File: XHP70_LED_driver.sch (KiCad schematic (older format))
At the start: 24 parts, among them U1 TPS61088, U2 INA181

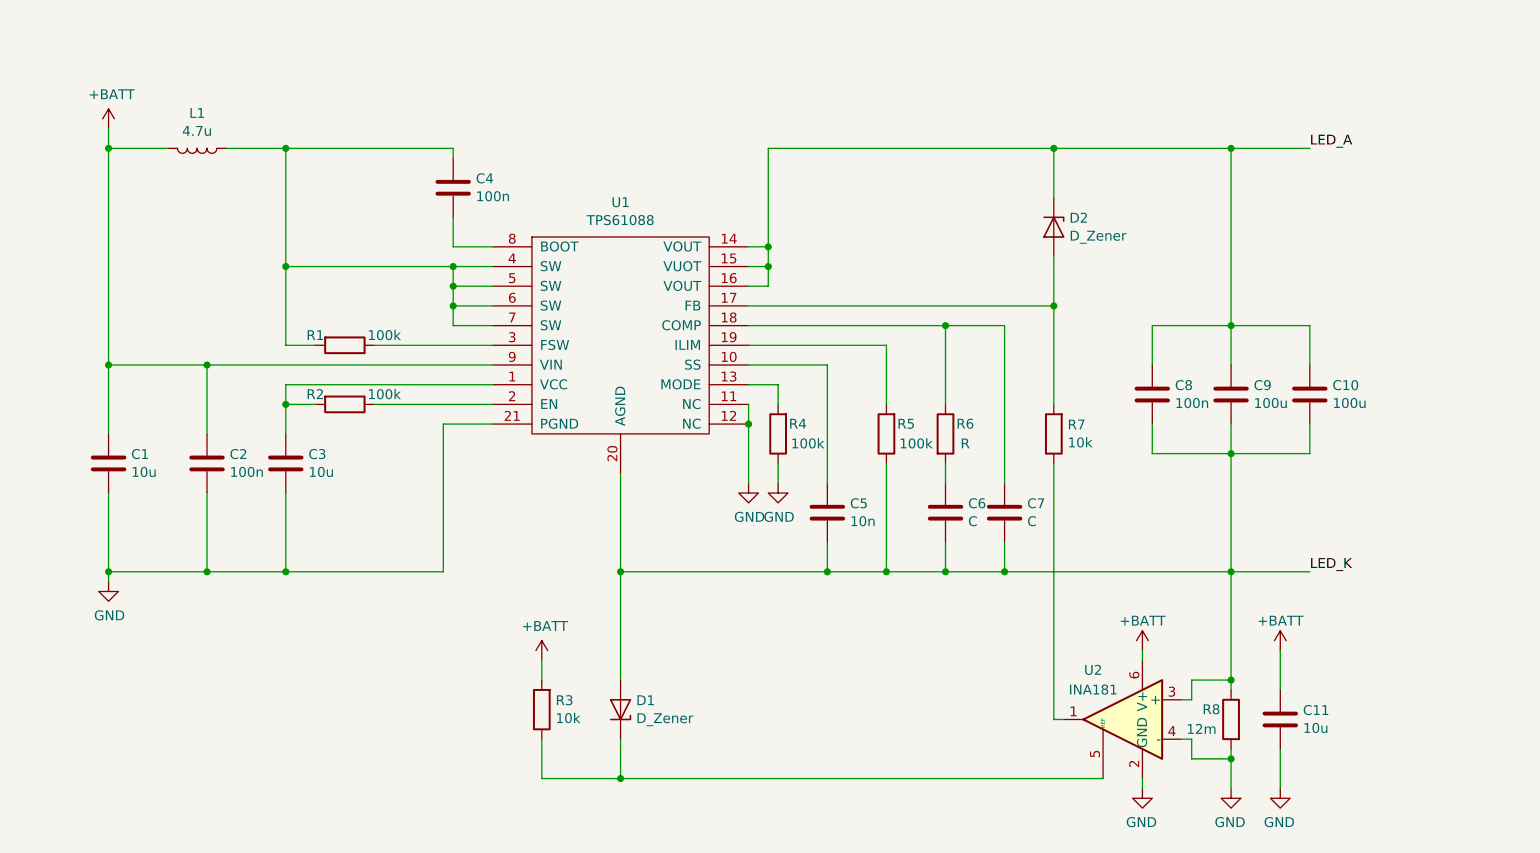
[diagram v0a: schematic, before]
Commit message: added microcontroller
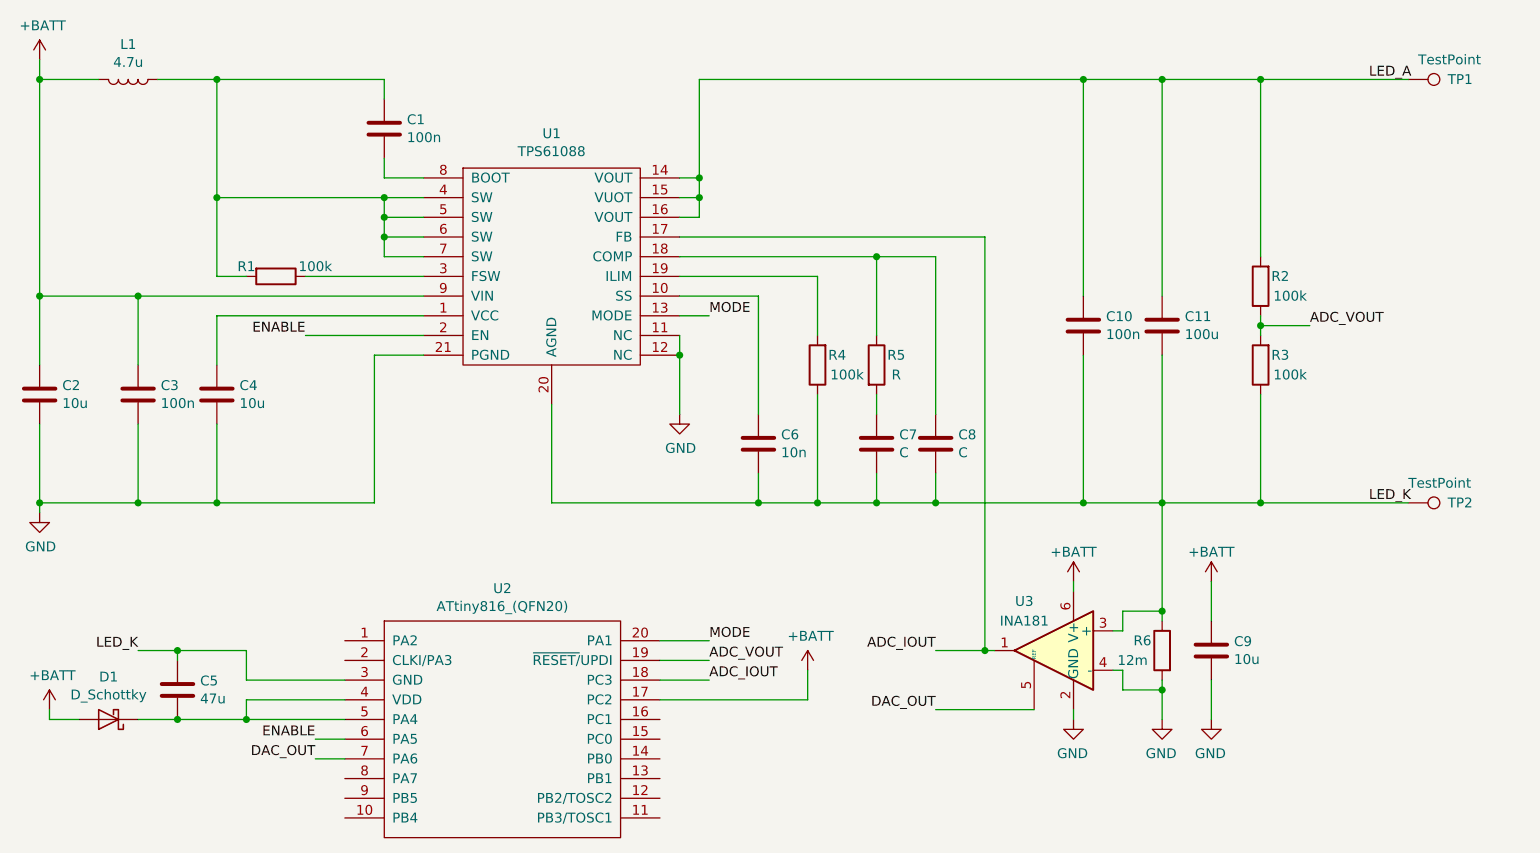
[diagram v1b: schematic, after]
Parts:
- removed C10: 100u, Capacitors_SMD:C_1210, symbol Device:C
- removed D1, D2: D_Zener, Diodes_SMD:D_SOD-123, symbol Device:D_Zener
- removed R4: 100k, Resistors_SMD:R_0402_NoSilk, symbol Device:R
- removed R7: 10k, Resistors_SMD:R_0402_NoSilk, symbol Device:R
- added C5: 47u, Capacitors_SMD:C_0805, symbol Device:C
- added D1: D_Schottky, Diodes_SMD:D_SOD-523, symbol Device:D_Schottky
- added TP1, TP2: TestPoint, Misc:flashlight_batt, symbol Connector:TestPoint
- added U2: ATtiny816_(QFN20), Housings_DFN_QFN:UQFN-20-1EP_3x3mm_Pitch0.4mm, symbol misc:ATtiny816_(QFN20)
- C2: renamed from C1; footprint Capacitors_SMD:C_1206 -> Capacitors_SMD:C_1210
- C3: renamed from C2; footprint Capacitors_SMD:C_0402_NoSilk -> Capacitors_SMD:C_0402
- C6: renamed from C5; footprint Capacitors_SMD:C_0402_NoSilk -> Capacitors_SMD:C_0402
- C7: renamed from C6; footprint Capacitors_SMD:C_0402_NoSilk -> Capacitors_SMD:C_0402
- C8: renamed from C7; footprint Capacitors_SMD:C_0402_NoSilk -> Capacitors_SMD:C_0402
- R3: value 10k -> 100k
- renumbered C4 to C1, C8 to C10, C9 to C11, C3 to C4, C11 to C9, R5 to R4, R6 to R5, R8 to R6, U2 to U3
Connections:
- net +BATT: now also D1.2 (A), U2.17 (PC2); no longer R3.2
- net LED_A: now also R2.2, TP1.1
- net LED_K: now also R3.1, C5.1, TP2.1, U2.3 (GND)
- net ADC_VOUT: now reaches R2.1
- net ADC_VOUT: now also R3.2, U2.19 (~RESET/~UPDI); no longer U1.2 (EN)
- net at C4.2, U1.1 (VCC): no longer R2.2
- net MODE: now reaches U1.13 (MODE)
- net MODE: now also U2.20 (PA1)
- net ADC_IOUT: now reaches U1.17 (FB)
- net ADC_IOUT: now also U3.1, U2.18 (PC3)
- net DAC_OUT: now reaches U3.5 (REF)
- net DAC_OUT: now also U2.7 (PA6); no longer R3.1
- new net: C5.2, D1.1 (K), U2.4 (VDD), U2.5 (PA4)
- new net ENABLE: U1.2 (EN), U2.6 (PA5)
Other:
- moved on the sheet: C1, C10, C11, C2, C3, C4, C6, C7, C8, C9, L1, R1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

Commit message: exported project milestone, fixed problems
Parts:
- added R7: 100k, Resistors_SMD:R_0402_NoSilk, symbol Device:R
- C7: value C -> 3.3nF
- C8: value C -> 100pF
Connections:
- net DAC_OUT: now also R7.1; no longer U3.5 (REF)
- new net: R7.2, U3.5 (REF)
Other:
- moved on the sheet: C10, C11, C8, C9, R2, R3, R6, TP1, TP2, U3

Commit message: finished, ready for prod.
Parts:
- removed TP1, TP2: TestPoint, Misc:flashlight_batt, symbol Connector:TestPoint
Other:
- moved on the sheet: C8, C9, R6, R7, U3
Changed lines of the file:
@@
 L Device:R R6
 U 1 1 5C24F41F
-P 8350 4800
-F 0 "R6" H 8450 4850 50  0000 C CNN
-F 1 "12m" H 8500 4750 50  0000 C CNN
-F 2 "Resistors_SMD:R_0805" V 8280 4800 50  0001 C CNN
-F 3 "~" H 8350 4800 50  0001 C CNN
-	1    8350 4800
+P 8700 4800
+F 0 "R6" H 8800 4850 50  0000 C CNN
+F 1 "12m" H 8850 4750 50  0000 C CNN
+F 2 "Resistors_SMD:R_0805" V 8630 4800 50  0001 C CNN
+F 3 "~" H 8700 4800 50  0001 C CNN
+	1    8700 4800
 	-1   0    0    -1
 $EndComp
@@
 L power:GND #PWR06
 U 1 1 5C24F4E2
-P 8350 5150
-F 0 "#PWR06" H 8350 4900 50  0001 C CNN
-F 1 "GND" H 8355 4977 50  0000 C CNN
-F 2 "" H 8350 5150 50  0001 C CNN
-F 3 "" H 8350 5150 50  0001 C CNN
-	1    8350 5150
+P 8700 5150
+F 0 "#PWR06" H 8700 4900 50  0001 C CNN
+F 1 "GND" H 8705 4977 50  0000 C CNN
+F 2 "" H 8700 5150 50  0001 C CNN
+F 3 "" H 8700 5150 50  0001 C CNN
+	1    8700 5150
 	-1   0    0    -1
 $EndComp
-Text Label 9250 1900 0    50   ~ 0
+Text Label 9450 1900 0    50   ~ 0
 LED_A
 Wire Wire Line
@@
 L Amplifier_Current:INA181 U3
 U 1 1 5C2D0B3D
-P 7800 4800
-F 0 "U3" H 7950 5050 50  0000 C CNN
-F 1 "INA181" H 7950 4950 50  0000 C CNN
-F 2 "TO_SOT_Packages_SMD:SOT-23-6" H 7850 4850 50  0001 C CNN
-F 3 "http://www.ti.com/lit/ds/symlink/ina181.pdf" H 7950 4950 50  0001 C CNN
-	1    7800 4800
+P 8150 4800
+F 0 "U3" H 8300 5050 50  0000 C CNN
+F 1 "INA181" H 8300 4950 50  0000 C CNN
+F 2 "TO_SOT_Packages_SMD:SOT-23-6" H 8200 4850 50  0001 C CNN
+F 3 "http://www.ti.com/lit/ds/symlink/ina181.pdf" H 8300 4950 50  0001 C CNN
+	1    8150 4800
 	-1   0    0    -1
 $EndComp
 Wire Wire Line
-	8150 4700 8100 4700
-Wire Wire Line
-	8150 4900 8150 5000
-Wire Wire Line
-	8350 4950 8350 5000
-Wire Wire Line
-	8350 5000 8150 5000
-Wire Wire Line
-	8350 4600 8150 4600
-Wire Wire Line
-	8350 4600 8350 4650
-Wire Wire Line
-	8150 4600 8150 4700
+	8500 4700 8450 4700
+Wire Wire Line
+	8500 4900 8500 5000
+Wire Wire Line
+	8700 4950 8700 5000
+Wire Wire Line
+	8700 5000 8500 5000
+Wire Wire Line
+	8700 4600 8500 4600
+Wire Wire Line
+	8700 4600 8700 4650
+Wire Wire Line
+	8500 4600 8500 4700
 $Comp
 L power:GND #PWR05
 U 1 1 5C2E6813
-P 7900 5150
-F 0 "#PWR05" H 7900 4900 50  0001 C CNN
-F 1 "GND" H 7905 4977 50  0000 C CNN
-F 2 "" H 7900 5150 50  0001 C CNN
-F 3 "" H 7900 5150 50  0001 C CNN
-	1    7900 5150
+P 8250 5150
+F 0 "#PWR05" H 8250 4900 50  0001 C CNN
+F 1 "GND" H 8255 4977 50  0000 C CNN
+F 2 "" H 8250 5150 50  0001 C CNN
+F 3 "" H 8250 5150 50  0001 C CNN
+	1    8250 5150
 	-1   0    0    -1
 $EndComp
 Wire Wire Line
-	8350 5150 8350 5000
-Connection ~ 8350 5000
+	8700 5150 8700 5000
+Connection ~ 8700 5000
 Wire Wire Line
 	6350 3500 6350 4050
-Text Label 9250 4050 0    50   ~ 0
+Text Label 9450 4050 0    50   ~ 0
 LED_K
 Wire Wire Line
-	7900 5150 7900 5100
+	8250 5150 8250 5100
 Wire Wire Line
 	3300 2900 3450 2900
@@
 	6050 3900 6050 4050
 Wire Wire Line
-	8100 4900 8150 4900
-Wire Wire Line
-	7450 4800 7500 4800
+	8450 4900 8500 4900
 Wire Wire Line
 	2400 3000 2400 3350
@@
 L power:+BATT #PWR04
 U 1 1 5C404A77
-P 7900 4450
-F 0 "#PWR04" H 7900 4300 50  0001 C CNN
-F 1 "+BATT" H 7900 4600 50  0000 C CNN
-F 2 "" H 7900 4450 50  0001 C CNN
-F 3 "" H 7900 4450 50  0001 C CNN
-	1    7900 4450
+P 8250 4450
+F 0 "#PWR04" H 8250 4300 50  0001 C CNN
+F 1 "+BATT" H 8250 4600 50  0000 C CNN
+F 2 "" H 8250 4450 50  0001 C CNN
+F 3 "" H 8250 4450 50  0001 C CNN
+	1    8250 4450
 	1    0    0    -1
 $EndComp
@@
 L Device:C C9
 U 1 1 5C411DA8
-P 8600 4800
-F 0 "C9" H 8485 4754 50  0000 R CNN
-F 1 "10u" H 8485 4845 50  0000 R CNN
-F 2 "Capacitors_SMD:C_0402" H 8638 4650 50  0001 C CNN
-F 3 "~" H 8600 4800 50  0001 C CNN
-	1    8600 4800
+P 8950 4800
+F 0 "C9" H 8835 4754 50  0000 R CNN
+F 1 "10u" H 8835 4845 50  0000 R CNN
+F 2 "Capacitors_SMD:C_0402" H 8988 4650 50  0001 C CNN
+F 3 "~" H 8950 4800 50  0001 C CNN
+	1    8950 4800
 	-1   0    0    1
 $EndComp
@@
 L power:GND #PWR08
 U 1 1 5C416F87
-P 8600 5150
-F 0 "#PWR08" H 8600 4900 50  0001 C CNN
-F 1 "GND" H 8605 4977 50  0000 C CNN
-F 2 "" H 8600 5150 50  0001 C CNN
-F 3 "" H 8600 5150 50  0001 C CNN
-	1    8600 5150
+P 8950 5150
+F 0 "#PWR08" H 8950 4900 50  0001 C CNN
+F 1 "GND" H 8955 4977 50  0000 C CNN
+F 2 "" H 8950 5150 50  0001 C CNN
+F 3 "" H 8950 5150 50  0001 C CNN
+	1    8950 5150
 	-1   0    0    -1
 $EndComp
@@
 L power:+BATT #PWR07
 U 1 1 5C41FECE
-P 8600 4450
-F 0 "#PWR07" H 8600 4300 50  0001 C CNN
-F 1 "+BATT" H 8600 4600 50  0000 C CNN
-F 2 "" H 8600 4450 50  0001 C CNN
-F 3 "" H 8600 4450 50  0001 C CNN
-	1    8600 4450
-	1    0    0    -1
-$EndComp
-Wire Wire Line
-	7900 4500 7900 4450
-Wire Wire Line
-	8600 4450 8600 4650
-Wire Wire Line
-	8600 4950 8600 5150
+P 8950 4450
+F 0 "#PWR07" H 8950 4300 50  0001 C CNN
+F 1 "+BATT" H 8950 4600 50  0000 C CNN
+F 2 "" H 8950 4450 50  0001 C CNN
+F 3 "" H 8950 4450 50  0001 C CNN
+	1    8950 4450
+	1    0    0    -1
+$EndComp
+Wire Wire Line
+	8250 4500 8250 4450
+Wire Wire Line
+	8950 4450 8950 4650
+Wire Wire Line
+	8950 4950 8950 5150
 Wire Wire Line
 	4350 2400 4150 2400
@@
 Connection ~ 8200 4050
 Wire Wire Line
-	8350 4050 8350 4600
-Connection ~ 8350 4600
+	8700 4050 8700 4600
+Connection ~ 8700 4600
 $Comp
 L tps61088:TPS61088 U1
@@
 L Device:C C8
 U 1 1 5C2566F7
-P 7050 3750
-F 0 "C8" H 6935 3704 50  0000 R CNN
-F 1 "100pF" H 6935 3795 50  0000 R CNN
-F 2 "Capacitors_SMD:C_0402" H 7088 3600 50  0001 C CNN
-F 3 "~" H 7050 3750 50  0001 C CNN
-	1    7050 3750
-	-1   0    0    1
-$EndComp
-Wire Wire Line
-	7050 3900 7050 4050
-Wire Wire Line
-	7050 3600 7050 2800
+P 7150 3750
+F 0 "C8" H 7035 3704 50  0000 R CNN
+F 1 "100pF" H 7035 3795 50  0000 R CNN
+F 2 "Capacitors_SMD:C_0402" H 7188 3600 50  0001 C CNN
+F 3 "~" H 7150 3750 50  0001 C CNN
+	1    7150 3750
+	-1   0    0    1
+$EndComp
+Wire Wire Line
+	7150 3900 7150 4050
+Wire Wire Line
+	7150 3600 7150 2800
 $Comp
 L power:GND #PWR0101
@@
 Wire Wire Line
 	5000 4050 6050 4050
-$Comp
-L Connector:TestPoint TP1
-U 1 1 5C26B3AB
-P 9450 1900
-F 0 "TP1" V 9450 2100 50  0000 L CNN
-F 1 "TestPoint" V 9350 1950 50  0000 L CNN
-F 2 "Misc:flashlight_batt" H 9650 1900 50  0001 C CNN
-F 3 "~" H 9650 1900 50  0001 C CNN
-	1    9450 1900
-	0    1    1    0
-$EndComp
 Connection ~ 8200 1900
-$Comp
-L Connector:TestPoint TP2
-U 1 1 5C26E8FF
-P 9450 4050
-F 0 "TP2" V 9450 4250 50  0000 L CNN
-F 1 "TestPoint" V 9350 4050 50  0000 L CNN
-F 2 "Misc:flashlight_batt" H 9650 4050 50  0001 C CNN
-F 3 "~" H 9650 4050 50  0001 C CNN
-	1    9450 4050
-	0    1    1    0
-$EndComp
 $Comp
 L misc:ATtiny816_(QFN20) U2
@@
 Text Label 3800 5350 2    50   ~ 0
 DAC_OUT
-Text Label 7100 5100 2    50   ~ 0
+Text Label 7450 5100 2    50   ~ 0
 DAC_OUT
-Text Label 7100 4800 2    50   ~ 0
+Text Label 7450 4800 2    50   ~ 0
 ADC_IOUT
-Connection ~ 7450 4800
 Wire Wire Line
 	3300 3100 3300 3350
@@
 	8200 1900 8700 1900
 Wire Wire Line
-	8200 4050 8350 4050
-Wire Wire Line
 	8700 3500 8700 4050
 Text Label 8950 3150 0    50   ~ 0
@@
 Wire Wire Line
 	3800 5350 3950 5350
-Wire Wire Line
-	7450 2700 7450 4800
 Wire Wire Line
 	2450 5100 2450 5150
@@
 Text Label 5800 3100 0    50   ~ 0
 MODE
-Text Label 5800 4750 0    50   ~ 0
+Text Label 5800 4650 0    50   ~ 0
 MODE
 Wire Wire Line
@@
 	3450 5150 3100 5150
 Connection ~ 3100 5150
-Wire Wire Line
-	5800 4750 5550 4750
 $Comp
 L power:+BATT #PWR0102
@@
 Wire Wire Line
 	5550 4950 5800 4950
-Wire Wire Line
-	5800 4850 5550 4850
 $Comp
 L Device:R R7
 U 1 1 5C454EBB
-P 7450 5100
-F 0 "R7" H 7350 5050 50  0000 C CNN
-F 1 "100k" H 7300 5150 50  0000 C CNN
-F 2 "Resistors_SMD:R_0402_NoSilk" V 7380 5100 50  0001 C CNN
-F 3 "~" H 7450 5100 50  0001 C CNN
-	1    7450 5100
+P 7800 5100
+F 0 "R7" H 7700 5050 50  0000 C CNN
+F 1 "100k" H 7650 5150 50  0000 C CNN
+F 2 "Resistors_SMD:R_0402_NoSilk" V 7730 5100 50  0001 C CNN
+F 3 "~" H 7800 5100 50  0001 C CNN
+	1    7800 5100
 	0    -1   -1   0
 $EndComp
 Wire Wire Line
-	7600 5100 7700 5100
+	7950 5100 8050 5100
 Wire Wire Line
 	5750 1900 7800 1900
 Wire Wire Line
-	7050 4050 7800 4050
-Connection ~ 7050 4050
-Wire Wire Line
-	7100 5100 7300 5100
+	7450 5100 7650 5100
 Wire Wire Line
 	7800 4050 8200 4050
-Wire Wire Line
-	6650 4050 7050 4050
 Connection ~ 6650 4050
 Wire Wire Line
-	6650 2800 7050 2800
-Connection ~ 8350 4050
-Wire Wire Line
-	8350 4050 8700 4050
-Wire Wire Line
-	5650 2700 7450 2700
-Wire Wire Line
-	7100 4800 7450 4800
+	5600 4750 5550 4750
+Text Label 5800 4750 0    50   ~ 0
+UPDI
+Wire Wire Line
+	5800 4650 5600 4650
+Wire Wire Line
+	5600 4650 5600 4750
+Wire Wire Line
+	5550 4850 5700 4850
+Wire Wire Line
+	5800 4750 5700 4750
+Wire Wire Line
+	5700 4750 5700 4850
+Connection ~ 5700 4850
+Wire Wire Line
+	5700 4850 5800 4850
+Wire Wire Line
+	8200 4050 8700 4050
+Wire Wire Line
+	7450 4800 7600 4800
+Wire Wire Line
+	7600 2700 7600 4800
+Wire Wire Line
+	5650 2700 7600 2700
+Connection ~ 7600 4800
+Wire Wire Line
+	7600 4800 7850 4800
+Connection ~ 7150 4050
+Wire Wire Line
+	7150 4050 7800 4050
+Wire Wire Line
+	6650 4050 7150 4050
+Wire Wire Line
+	6650 2800 7150 2800
 $EndSCHEMATC
